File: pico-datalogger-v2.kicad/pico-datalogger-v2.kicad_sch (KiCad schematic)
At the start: 31 parts, among them J1 JST-PH2 Bat, J10 Conn_PCB_2, J11 Conn_I2C1, J12 Conn_UART, J2 Conn_Pico_Left, J3 Conn_Pico_Right, J4 Alt-Bat, J5 Conn_LoRa, J6 Conn_Display, J7 Conn_PCB_1, J8 Conn_ADC, J9 Conn_I2C0, Q1 AO3401A, U1 74LVC2G74, U2 PCF8523T, U3 Pico, U4 XTSD, Y1 Crystal

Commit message: preliminary routing
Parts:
- J12: value Conn_UART -> Conn_UART_5V
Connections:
- net +3V3: no longer J12.2 (Pin_2)
- net Display_BUSY: now also J6.4 (Pin_4); no longer J6.3 (Pin_3)
- net Display_RST: now also J6.3 (Pin_3); no longer J6.4 (Pin_4)
- net GND: now also J12.3 (Pin_3); no longer J12.1 (Pin_1)
- net Lora_CS: now also J2.17 (Pin_17), J5.5 (Pin_5), U3.17 (GPIO13); no longer J2.12 (Pin_12), J5.2 (Pin_2), U3.12 (GPIO9)
- net Lora_RST: now also J2.16 (Pin_16), J5.4 (Pin_4), U3.16 (GPIO12); no longer J2.10 (Pin_10), J5.1 (Pin_1), U3.10 (GPIO7)
- net MISO1: now also J5.1 (Pin_1); no longer J5.4 (Pin_4)
- net PDM_DAT: now also J10.3 (Pin_3); no longer J10.2 (Pin_2)
- net RX: now also J12.1 (Pin_1); no longer J12.4 (Pin_4)
- net SCL: now also J10.6 (Pin_6); no longer J10.4 (Pin_4)
- net SCLK1: now also J5.2 (Pin_2); no longer J5.5 (Pin_5)
- net SDA: now also J10.5 (Pin_5); no longer J10.3 (Pin_3)
- net SWA: now also J10.4 (Pin_4), J2.10 (Pin_10), U3.10 (GPIO7); no longer J10.6 (Pin_6), J2.16 (Pin_16), U3.16 (GPIO12)
- net SWB: now also J2.12 (Pin_12), U3.12 (GPIO9); no longer J2.17 (Pin_17), U3.17 (GPIO13)
- net SWD: now also J10.2 (Pin_2); no longer J10.5 (Pin_5)
- net TX: now also J12.2 (Pin_2); no longer J12.3 (Pin_3)
- net VBUS: now reaches J3.1 (Pin_1)
- net VBUS: now also J12.4 (Pin_4), U3.40 (VBUS)
- no-connect marks 8 -> 6
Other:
- moved on the sheet: J12
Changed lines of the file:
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@@
   (title_block
     (title "pico-datalogger-v2")
-    (date "2023-08-12")
-    (rev "0.9")
+    (date "2023-08-17")
+    (rev "0.91")
     (company "Bernhard Bablok")
     (comment 1 "https://github.com/bablokb/pcb-pico-datalogger")
@@
   (no_connect (at 86.106 132.588))
   (no_connect (at 241.3 150.114))
-  (no_connect (at 91.948 28.702))
-  (no_connect (at 86.106 119.888))
   (wire (pts (xy 151.13 76.962) (xy 144.526 76.962))
     (stroke (width 0) (type default) (color 0 0 0 0))
@@
     (stroke (width 0) (type default) (color 0 0 0 0))
   )
+  (wire (pts (xy 161.544 122.936) (xy 164.846 122.936))
+    (stroke (width 0) (type default) (color 0 0 0 0))
+  )
   (wire (pts (xy 256.032 86.106) (xy 264.16 86.106))
     (stroke (width 0) (type default) (color 0 0 0 0))
@@
     (stroke (width 0) (type default) (color 0 0 0 0))
   )
-  (wire (pts (xy 164.846 122.936) (xy 161.544 122.936))
-    (stroke (width 0) (type default) (color 0 0 0 0))
-  )
   (wire (pts (xy 176.276 96.012) (xy 176.276 98.298))
     (stroke (width 0) (type default) (color 0 0 0 0))
@@
     (stroke (width 0) (type default) (color 0 0 0 0))
   )
+  (wire (pts (xy 98.298 28.702) (xy 91.948 28.702))
+    (stroke (width 0) (type default) (color 0 0 0 0))
+  )
   (wire (pts (xy 94.488 33.782) (xy 94.488 46.482))
     (stroke (width 0) (type default) (color 0 0 0 0))
@@
     (stroke (width 0) (type default) (color 0 0 0 0))
   )
+  (wire (pts (xy 161.544 117.856) (xy 164.846 117.856))
+    (stroke (width 0) (type default) (color 0 0 0 0))
+  )
   (wire (pts (xy 242.57 48.768) (xy 236.982 48.768))
     (stroke (width 0) (type default) (color 0 0 0 0))
@@
     (stroke (width 0) (type default) (color 0 0 0 0))
   )
+  (wire (pts (xy 94.742 119.888) (xy 86.106 119.888))
+    (stroke (width 0) (type default) (color 0 0 0 0))
+  )
   (wire (pts (xy 147.32 29.845) (xy 149.86 29.845))
     (stroke (width 0) (type default) (color 0 0 0 0))
@@
     (stroke (width 0) (type default) (color 0 0 0 0))
   )
-  (wire (pts (xy 164.846 125.476) (xy 161.544 125.476))
+  (wire (pts (xy 161.544 125.476) (xy 164.846 125.476))
     (stroke (width 0) (type default) (color 0 0 0 0))
   )
@@
     (effects (font (size 1.27 1.27)) (justify left bottom))
   )
-  (label "SWD" (at 179.324 151.638 180)
+  (label "SWD" (at 179.324 144.018 180)
     (effects (font (size 1.27 1.27)) (justify right bottom))
   )
@@
     (effects (font (size 1.27 1.27)) (justify left bottom))
   )
+  (label "VBUS" (at 98.298 28.702 0)
+    (effects (font (size 1.27 1.27)) (justify left bottom))
+  )
   (label "SDA" (at 52.07 36.322 180)
     (effects (font (size 1.27 1.27)) (justify right bottom))
@@
     (effects (font (size 1.27 1.27)) (justify left bottom))
   )
-  (label "Lora_RST" (at 141.732 108.712 0)
+  (label "Lora_RST" (at 141.732 116.332 0)
     (effects (font (size 1.27 1.27)) (justify left bottom))
   )
-  (label "Display_RST" (at 181.864 115.824 180)
+  (label "Display_RST" (at 182.118 113.284 180)
     (effects (font (size 1.27 1.27)) (justify right bottom))
   )
@@
     (effects (font (size 1.27 1.27)) (justify left bottom))
   )
-  (label "SCLK1" (at 141.732 118.872 0)
+  (label "SCLK1" (at 141.732 111.252 0)
     (effects (font (size 1.27 1.27)) (justify left bottom))
   )
@@
     (effects (font (size 1.27 1.27)) (justify right bottom))
   )
-  (label "Lora_RST" (at 52.07 51.562 180)
+  (label "Lora_RST" (at 51.816 66.802 180)
     (effects (font (size 1.27 1.27)) (justify right bottom))
   )
@@
     (effects (font (size 1.27 1.27)) (justify left bottom))
   )
+  (label "VBUS" (at 94.742 119.888 0)
+    (effects (font (size 1.27 1.27)) (justify left bottom))
+  )
   (label "SD_CS" (at 99.06 56.642 0)
     (effects (font (size 1.27 1.27)) (justify left bottom))
   )
-  (label "SWA" (at 53.594 157.988 180)
+  (label "SWA" (at 54.356 142.748 180)
     (effects (font (size 1.27 1.27)) (justify right bottom))
   )
@@
     (effects (font (size 1.27 1.27)) (justify right bottom))
   )
-  (label "Lora_CS" (at 141.732 111.252 0)
+  (label "Lora_CS" (at 141.732 118.872 0)
     (effects (font (size 1.27 1.27)) (justify left bottom))
   )
@@
     (effects (font (size 1.27 1.27)) (justify right bottom))
   )
-  (label "Lora_RST" (at 54.356 142.748 180)
+  (label "Lora_RST" (at 53.594 157.988 180)
     (effects (font (size 1.27 1.27)) (justify right bottom))
   )
@@
     (effects (font (size 1.27 1.27)) (justify left bottom))
   )
-  (label "SCL" (at 179.324 149.098 180)
+  (label "SCL" (at 179.324 154.178 180)
     (effects (font (size 1.27 1.27)) (justify right bottom))
   )
@@
     (effects (font (size 1.27 1.27)) (justify right bottom))
   )
-  (label "MISO1" (at 141.732 116.332 0)
+  (label "MISO1" (at 141.732 108.712 0)
     (effects (font (size 1.27 1.27)) (justify left bottom))
   )
@@
     (effects (font (size 1.27 1.27)) (justify right bottom))
   )
-  (label "Display_BUSY" (at 182.118 113.284 180)
+  (label "VBUS" (at 164.846 117.856 0)
+    (effects (font (size 1.27 1.27)) (justify left bottom))
+  )
+  (label "Display_BUSY" (at 181.864 115.824 180)
     (effects (font (size 1.27 1.27)) (justify right bottom))
   )
@@
     (effects (font (size 1.27 1.27)) (justify right bottom))
   )
-  (label "PDM_DAT" (at 179.324 144.018 180)
+  (label "PDM_DAT" (at 179.07 146.558 180)
     (effects (font (size 1.27 1.27)) (justify right bottom))
   )
-  (label "SWB" (at 51.816 69.342 180)
+  (label "SWB" (at 52.07 56.642 180)
     (effects (font (size 1.27 1.27)) (justify right bottom))
   )
@@
     (effects (font (size 1.27 1.27)) (justify right bottom))
   )
-  (label "Lora_CS" (at 52.07 56.642 180)
+  (label "Lora_CS" (at 51.816 69.342 180)
     (effects (font (size 1.27 1.27)) (justify right bottom))
   )
@@
     (effects (font (size 1.27 1.27)) (justify right bottom))
   )
-  (label "SWA" (at 51.816 66.802 180)
+  (label "SWA" (at 52.07 51.562 180)
     (effects (font (size 1.27 1.27)) (justify right bottom))
   )
-  (label "SDA" (at 179.07 146.558 180)
+  (label "SDA" (at 179.324 151.638 180)
     (effects (font (size 1.27 1.27)) (justify right bottom))
   )
@@
     (effects (font (size 1.27 1.27)) (justify left bottom))
   )
-  (label "Lora_CS" (at 53.848 147.828 180)
+  (label "Lora_CS" (at 53.594 160.528 180)
     (effects (font (size 1.27 1.27)) (justify right bottom))
   )
@@
     (effects (font (size 1.27 1.27)) (justify left bottom))
   )
-  (label "SWA" (at 179.324 154.178 180)
+  (label "SWA" (at 179.324 149.098 180)
     (effects (font (size 1.27 1.27)) (justify right bottom))
   )
@@
     (effects (font (size 1.27 1.27)) (justify left bottom))
   )
-  (label "SWB" (at 53.594 160.528 180)
+  (label "SWB" (at 53.848 147.828 180)
     (effects (font (size 1.27 1.27)) (justify right bottom))
   )
@@
     (pin "2")
   )
-  (symbol (lib_id "power:GND") (at 161.544 117.856 90) (unit 1)
+  (symbol (lib_id "power:GND") (at 161.544 120.396 90) (unit 1)
     (in_bom yes) (on_board yes)
-    (property "Reference" "#PWR024" (id 0) (at 167.894 117.856 0)
+    (property "Reference" "#PWR024" (id 0) (at 167.894 120.396 0)
       (effects (font (size 1.27 1.27)) hide)
     )
-    (property "Value" "GND" (id 1) (at 168.656 117.856 90)
+    (property "Value" "GND" (id 1) (at 168.656 119.888 90)
       (effects (font (size 1.27 1.27)) (justify left))
     )
-    (property "Footprint" "" (id 2) (at 161.544 117.856 0)
+    (property "Footprint" "" (id 2) (at 161.544 120.396 0)
       (effects (font (size 1.27 1.27)) hide)
     )
-    (property "Datasheet" "" (id 3) (at 161.544 117.856 0)
+    (property "Datasheet" "" (id 3) (at 161.544 120.396 0)
       (effects (font (size 1.27 1.27)) hide)
     )
@@
     (pin "1")
   )
-  (symbol (lib_id "power:+3V3") (at 161.544 120.396 270) (unit 1)
-    (in_bom yes) (on_board yes)
-    (property "Reference" "#PWR031" (id 0) (at 157.734 120.396 0)
-      (effects (font (size 1.27 1.27)) hide)
-    )
-    (property "Value" "+3V3" (id 1) (at 169.418 120.396 90)
-      (effects (font (size 1.27 1.27)) (justify right))
-    )
-    (property "Footprint" "" (id 2) (at 161.544 120.396 0)
-      (effects (font (size 1.27 1.27)) hide)
-    )
-    (property "Datasheet" "" (id 3) (at 161.544 120.396 0)
-      (effects (font (size 1.27 1.27)) hide)
-    )
-    (pin "1")
-  )
-  (symbol (lib_id "Connector_Generic:Conn_01x04") (at 156.464 120.396 0) (mirror y) (unit 1)
+  (symbol (lib_id "Connector_Generic:Conn_01x04") (at 156.464 122.936 180) (unit 1)
     (in_bom yes) (on_board yes)
     (property "Reference" "J12" (id 0) (at 156.718 111.76 0))
-    (property "Value" "Conn_UART" (id 1) (at 156.972 114.3 0))
-    (property "Footprint" "Connector_PinHeader_2.54mm:PinHeader_1x04_P2.54mm_Horizontal" (id 2) (at 156.464 120.396 0)
+    (property "Value" "Conn_UART_5V" (id 1) (at 156.972 114.3 0))
+    (property "Footprint" "Connector_PinHeader_2.54mm:PinHeader_1x04_P2.54mm_Horizontal" (id 2) (at 156.464 122.936 0)
       (effects (font (size 1.27 1.27)) hide)
     )
-    (property "Datasheet" "~" (id 3) (at 156.464 120.396 0)
+    (property "Datasheet" "~" (id 3) (at 156.464 122.936 0)
       (effects (font (size 1.27 1.27)) hide)
     )
@@
       (reference "#PWR028") (unit 1) (value "GND") (footprint "")
     )
-    (path "/f2b8183f-318e-421b-9d0a-79de8fbdc62b"
-      (reference "#PWR031") (unit 1) (value "+3V3") (footprint "")
-    )
     (path "/ac7dda72-ef93-47f8-ba8e-cc7eb10e88fc"
       (reference "#PWR0101") (unit 1) (value "+3V3") (footprint "")
@@
     )
     (path "/f4141f83-f28d-484e-84bb-e85ebfe1aae8"
-      (reference "J12") (unit 1) (value "Conn_UART") (footprint "Connector_PinHeader_2.54mm:PinHeader_1x04_P2.54mm_Horizontal")
+      (reference "J12") (unit 1) (value "Conn_UART_5V") (footprint "Connector_PinHeader_2.54mm:PinHeader_1x04_P2.54mm_Horizontal")
     )
     (path "/a2bbecfe-02e1-46bb-a8e7-6ba53ada3091"

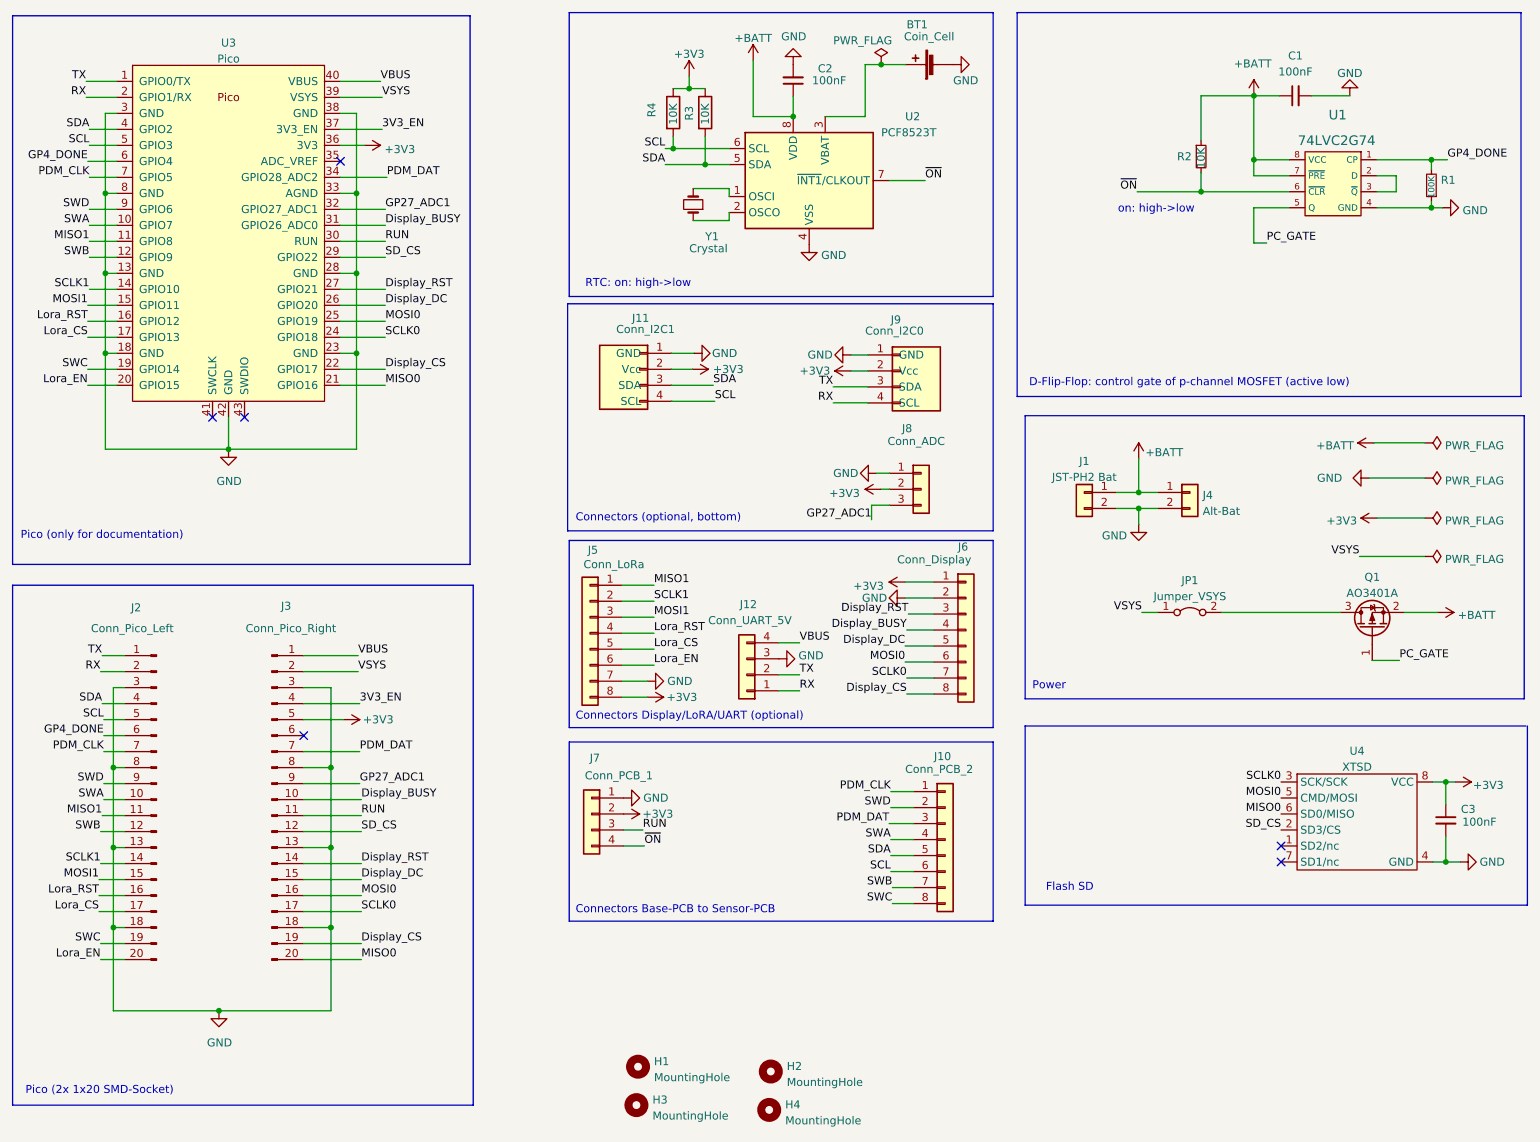
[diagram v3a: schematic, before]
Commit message: added some more optional components (buttons, I2C-connector)
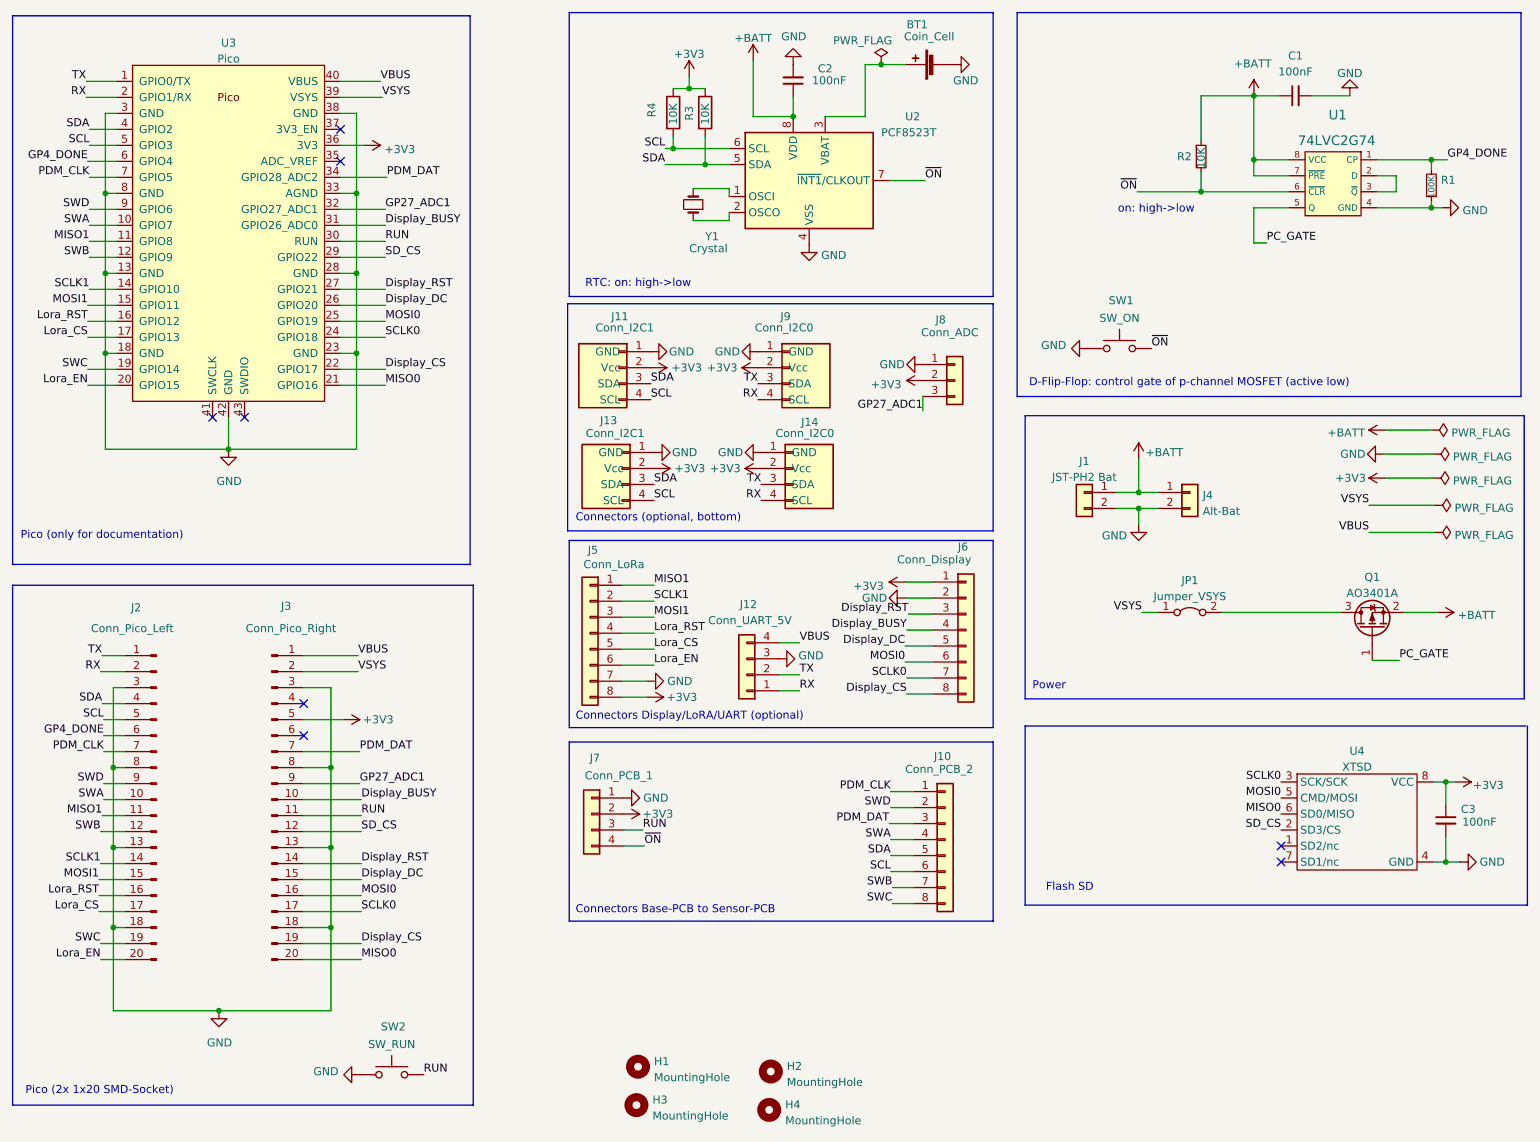
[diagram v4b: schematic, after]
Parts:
- added J13: Conn_I2C1, Connector_PinHeader_2.54mm:PinHeader_1x04_P2.54mm_Vertical, symbol user:Stemma-QT_Qwicc
- added J14: Conn_I2C0, Connector_PinHeader_2.54mm:PinHeader_1x04_P2.54mm_Vertical, symbol user:Stemma-QT_Qwicc
- added SW1: SW_ON, user:SW_PUSH_1x_6mm, symbol Switch:SW_Push
- added SW2: SW_RUN, user:SW_PUSH_1x_6mm, symbol Switch:SW_Push
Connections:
- net +3V3: now also J13.2 (Vcc), J14.2 (Vcc)
- net GND: now also J13.1 (GND), J14.1 (GND), SW1.1, SW2.1
- net RUN: now also SW2.2
- net RX: now also J14.4 (SCL)
- net SCL: now also J13.4 (SCL)
- net SDA: now also J13.3 (SDA)
- net TX: now also J14.3 (SDA)
- net ~{ON}: now also SW1.2
- net 3V3_EN: no longer names the net of J3.4 (Pin_4)
- net 3V3_EN: no longer U3.37 (3V3_EN)
- no-connect marks 6 -> 8
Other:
- moved on the sheet: J11, J8, J9
